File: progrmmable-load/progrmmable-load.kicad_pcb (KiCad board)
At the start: 2 copper layers, 99.1 x 50.8 mm, 32 parts, among them J1 Screw_Terminal_01x02, J2 Conn_01x02, Q1 IRLZ44N, SW1 Rotary_Encoder, U1 MCP4725A2T-E_CH, U2 AD8608ARZ-REEL

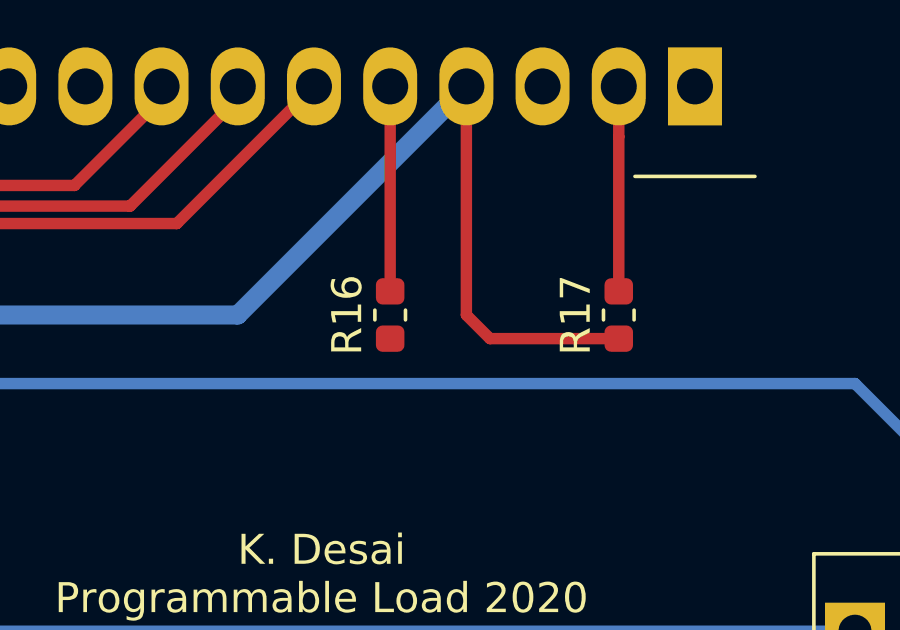
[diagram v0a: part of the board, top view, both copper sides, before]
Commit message: Add R18 to fix LCD contrast
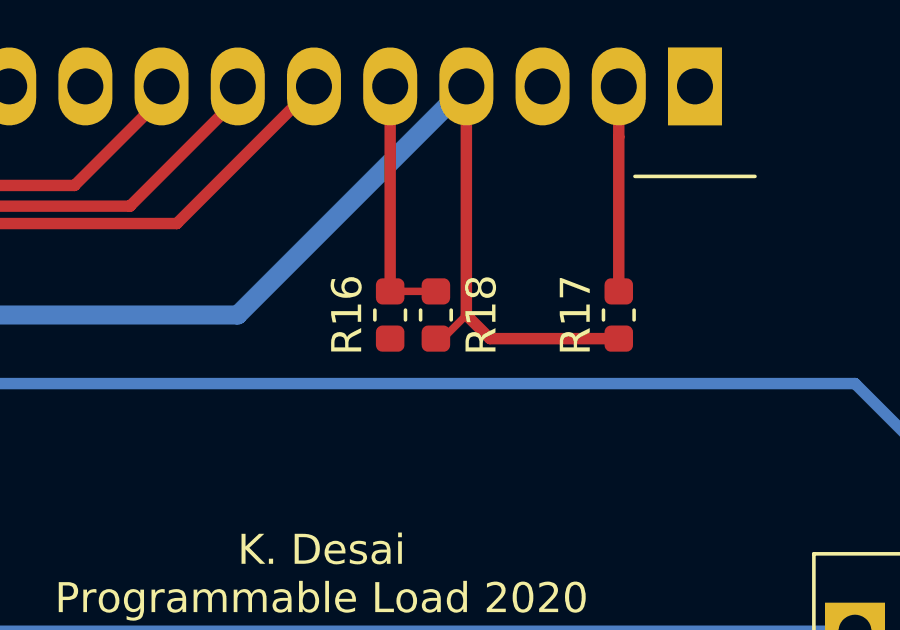
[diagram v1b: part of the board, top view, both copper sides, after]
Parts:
- added R18: 2k, Resistor_SMD:R_0603_1608Metric, F.Cu at (167.6, 108.8)
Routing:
- net Net-(DS1-Pad5): track 6.83 -> 8.36 mm
- net +5V: track 112.1 -> 113.5 mm
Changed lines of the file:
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@@
     (thickness 1.6)
     (drawings 105)
-    (tracks 173)
+    (tracks 176)
     (zones 0)
-    (modules 32)
+    (modules 33)
     (nets 50)
   )
@@
     (add_net "Net-(R7-Pad1)")
     (add_net "Net-(U2-Pad1)")
+  )
+  (module Resistor_SMD:R_0603_1608Metric (layer F.Cu)
+    (at 167.64 108.839 90)
+    (descr "Resistor SMD 0603 (1608 Metric), square (rectangular) end terminal, IPC_7351 nominal, (Body size source: http://www.tortai-tech.com/upload/download/2011102023233369053.pdf), generated with kicad-footprint-generator")
+    (tags resistor)
+    (attr smd)
+    (fp_text reference R18 (at 0 1.524 90) (layer F.SilkS)
+      (effects (font (size 1 1) (thickness 0.15)))
+    )
+    (fp_text value 2k (at 0 1.43 90) (layer F.Fab)
+      (effects (font (size 1 1) (thickness 0.15)))
+    )
+    (fp_text user %R (at 0 0 90) (layer F.Fab)
+      (effects (font (size 0.4 0.4) (thickness 0.06)))
+    )
+    (fp_line (start 1.48 0.73) (end -1.48 0.73) (layer F.CrtYd) (width 0.05))
+    (fp_line (start 1.48 -0.73) (end 1.48 0.73) (layer F.CrtYd) (width 0.05))
+    (fp_line (start -1.48 -0.73) (end 1.48 -0.73) (layer F.CrtYd) (width 0.05))
+    (fp_line (start -1.48 0.73) (end -1.48 -0.73) (layer F.CrtYd) (width 0.05))
+    (fp_line (start -0.162779 0.51) (end 0.162779 0.51) (layer F.SilkS) (width 0.12))
+    (fp_line (start -0.162779 -0.51) (end 0.162779 -0.51) (layer F.SilkS) (width 0.12))
+    (fp_line (start 0.8 0.4) (end -0.8 0.4) (layer F.Fab) (width 0.1))
+    (fp_line (start 0.8 -0.4) (end 0.8 0.4) (layer F.Fab) (width 0.1))
+    (fp_line (start -0.8 -0.4) (end 0.8 -0.4) (layer F.Fab) (width 0.1))
+    (fp_line (start -0.8 0.4) (end -0.8 -0.4) (layer F.Fab) (width 0.1))
+    (pad 2 smd roundrect (at 0.7875 0 90) (size 0.875 0.95) (layers F.Cu F.Paste F.Mask) (roundrect_rratio 0.25)
+      (net 46 "Net-(DS1-Pad5)"))
+    (pad 1 smd roundrect (at -0.7875 0 90) (size 0.875 0.95) (layers F.Cu F.Paste F.Mask) (roundrect_rratio 0.25)
+      (net 9 +5V))
+    (model ${KISYS3DMOD}/Resistor_SMD.3dshapes/R_0603_1608Metric.wrl
+      (at (xyz 0 0 0))
+      (scale (xyz 1 1 1))
+      (rotate (xyz 0 0 0))
+    )
   )
   (module Display:HY1602E (layer F.Cu)
@@
   (segment (start 127.924509 128.716991) (end 127.9905 128.651) (width 0.381) (layer F.Cu) (net 9))
   (segment (start 125.7554 128.716991) (end 127.924509 128.716991) (width 0.381) (layer F.Cu) (net 9))
+  (segment (start 167.8685 109.6265) (end 168.656 108.839) (width 0.25) (layer F.Cu) (net 9))
+  (segment (start 167.64 109.6265) (end 167.8685 109.6265) (width 0.25) (layer F.Cu) (net 9))
   (segment (start 121.412 127.69) (end 121.412 127.1525) (width 0.381) (layer F.Cu) (net 13))
   (segment (start 121.412 128.607093) (end 121.412 127.69) (width 0.381) (layer F.Cu) (net 13))
@@
   (segment (start 136.9822 119.507) (end 136.9822 120.777) (width 0.381) (layer F.Cu) (net 41))
   (segment (start 166.116 101.219) (end 166.116 108.0515) (width 0.381) (layer F.Cu) (net 46))
+  (segment (start 167.64 108.0515) (end 166.116 108.0515) (width 0.25) (layer F.Cu) (net 46))
   (segment (start 173.736 102.9) (end 173.736 108.0515) (width 0.381) (layer F.Cu) (net 47))
   (segment (start 173.736 101.219) (end 173.736 102.9) (width 0.381) (layer F.Cu) (net 47))
